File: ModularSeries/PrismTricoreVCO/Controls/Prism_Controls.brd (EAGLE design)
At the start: 48.5 x 100 mm, 10 parts

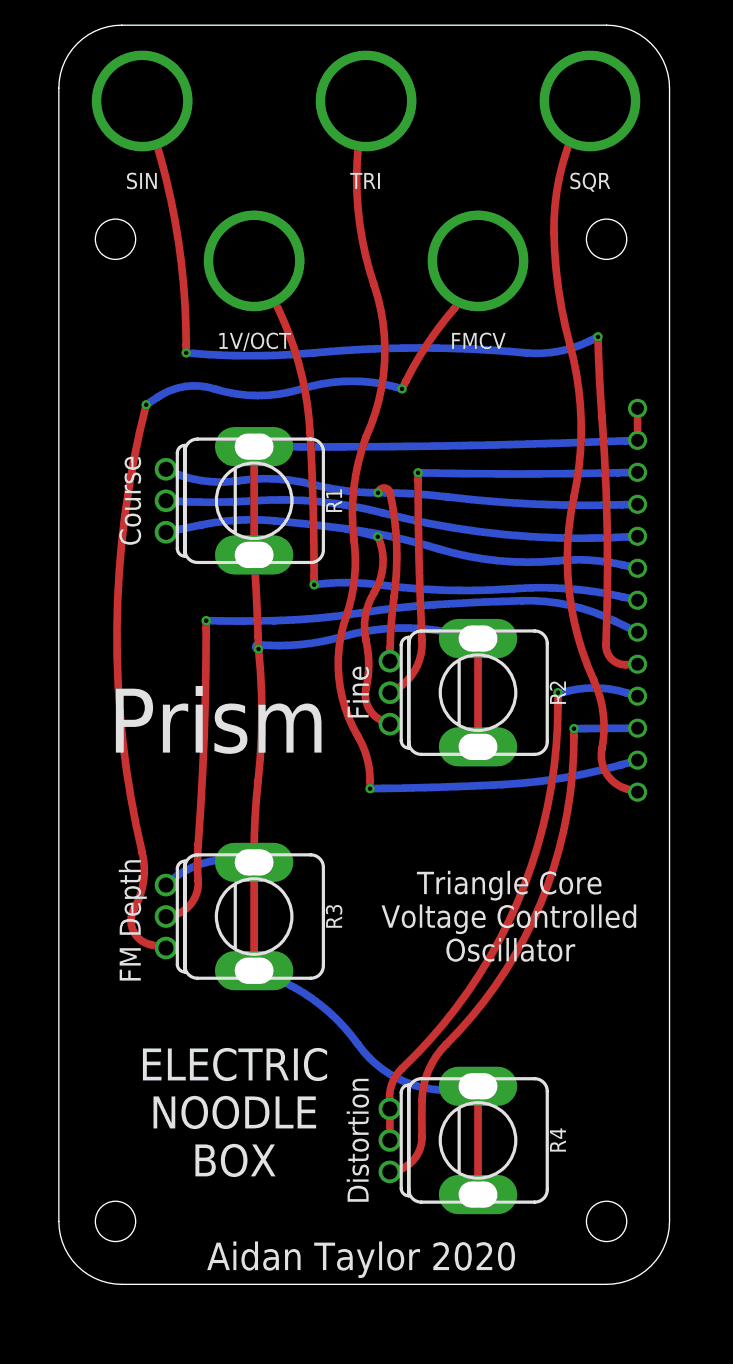
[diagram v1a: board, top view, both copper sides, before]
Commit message: Prism control card updated to accomodate Cinch nanas
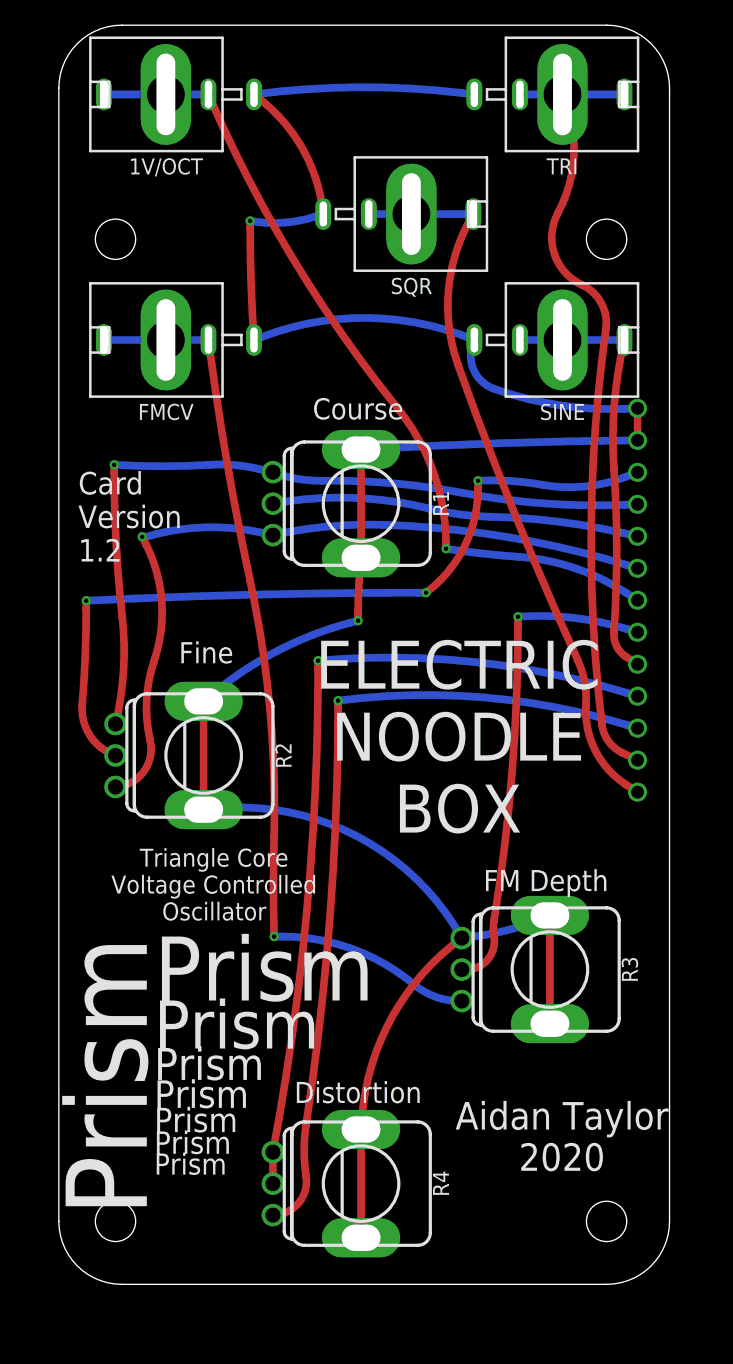
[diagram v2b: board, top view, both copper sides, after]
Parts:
- removed SIN: BANANA_PANEL, ElectricNoodleBox:BANANA_PANEL
- added SINE: COMBI-JACKCINCHNANA, ElectricNoodleBox:NEWCOMBOJACK_PANEL
- 1V/OCT, FMCV, SQR, TRI: value BANANA_PANEL -> COMBI-JACKCINCHNANA; device ElectricNoodleBox:BANANA_PANEL -> ElectricNoodleBox:NEWCOMBOJACK_PANEL
- moved FMCV 25.6 mm to (9.50, 75.0), turned to 90 degrees
- moved R3 23.9 mm to (40.0, 25.0)
- moved R2 22.4 mm to (12.5, 42.0)
- moved SQR 16.8 mm to (29.0, 85.0), turned to 270 degrees
- moved TRI 15.6 mm to (41.0, 94.5), turned to 270 degrees
- moved 1V/OCT 15.0 mm to (9.50, 94.5), turned to 90 degrees
- moved R4 9.90 mm to (25.0, 8.00)
- moved R1 8.49 mm to (25.0, 62.0)
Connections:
- net AGND: now also 1V/OCT.S, FMCV.S, SINE.S, SQR.S, TRI.S
- net N$1: now also 1V/OCT.T1, 1V/OCT.T2
- net N$10: now also SINE.CONN, SINE.T1, SINE.T2; no longer SIN.CONN
- net N$11: now also TRI.T1, TRI.T2
- net N$12: now also SQR.T1, SQR.T2
- net N$6: now also FMCV.T1, FMCV.T2
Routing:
- net AGND: track 137.4 -> 202.4 mm, vias 1 -> 2
- net N$10: track 80.8 -> 34.8 mm, vias 2 -> 0
- net N$5: track 35.6 -> 62.7 mm, vias 1 -> 3
- net N$8: track 44.6 -> 67.2 mm
- net N$9: track 43.7 -> 65.8 mm
- net N$7: track 59.2 -> 38.7 mm
- net N$11: track 76.3 -> 63.3 mm, vias 1 -> 0
- net N$1: track 52.2 -> 65.1 mm
- net N$2: track 51.9 -> 62.4 mm
- net N$4: track 37.6 -> 29.1 mm
- net N$6: track 76.9 -> 71.8 mm, vias 2 -> 1
- net N$3: track 56.1 -> 60.6 mm
- net N$12: track 56.7 -> 57.4 mm
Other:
- board text added: "Card Version 1.2"

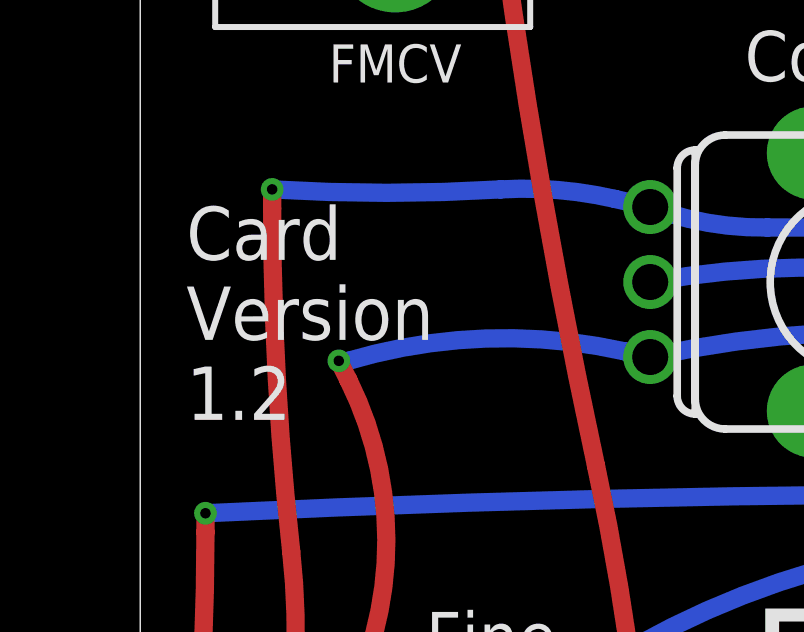
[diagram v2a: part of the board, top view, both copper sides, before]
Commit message: Updates to Portals and Knives, Panel layout for Prism and Knives added
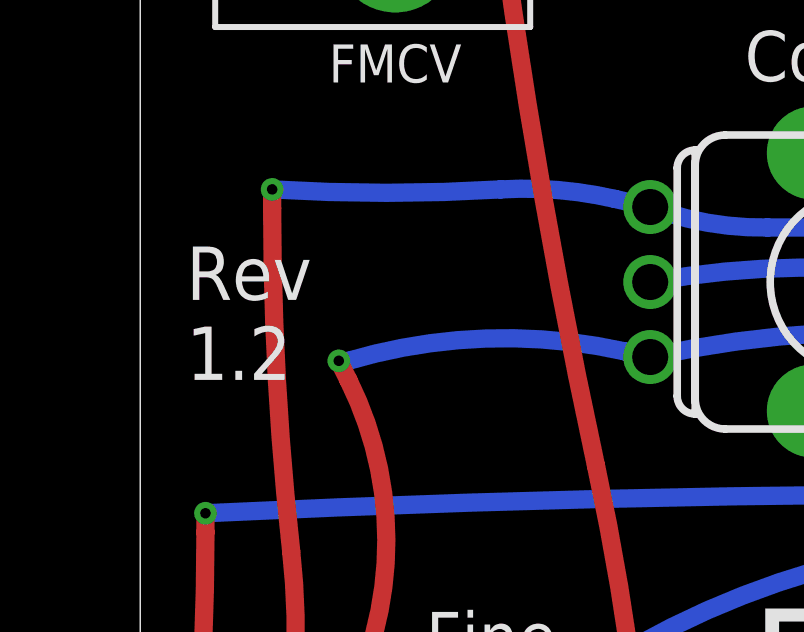
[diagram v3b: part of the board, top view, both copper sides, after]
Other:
- board text added: "Rev 1.2"
- board text removed: "Card Version 1.2"
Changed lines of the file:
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@@
 <setting verticaltext="up"/>
 </settings>
-<grid distance="12.5" unitdist="mil" unit="mil" style="lines" multiple="1" display="no" altdistance="5" altunitdist="mil" altunit="mil"/>
+<grid distance="12.5" unitdist="mil" unit="mm" style="lines" multiple="1" display="no" altdistance="5" altunitdist="mil" altunit="mil"/>
 <layers>
 <layer number="1" name="Top" color="4" fill="1" visible="yes" active="yes"/>
@@
 <layer number="44" name="Drills" color="7" fill="1" visible="no" active="yes"/>
 <layer number="45" name="Holes" color="7" fill="1" visible="no" active="yes"/>
-<layer number="46" name="Milling" color="3" fill="1" visible="no" active="yes"/>
+<layer number="46" name="Milling" color="3" fill="1" visible="yes" active="yes"/>
 <layer number="47" name="Measures" color="7" fill="1" visible="no" active="yes"/>
 <layer number="48" name="Document" color="7" fill="1" visible="yes" active="yes"/>
@@
 </layers>
 <board>
-<fusionsync huburn="a.cGVyc29uYWw6dWUyYjdlNGE0" projecturn="a.cGVyc29uYWw6dWUyYjdlNGE0IzIwMjAwNDA1MjgzMzA0MTgx" f3durn="urn:adsk.wipprod:dm.lineage:eztbtJ9iQJeDtqV6BqPWgw" pcbguid="61dd8330-7d56-4479-a556-bfe94448c2a6" lastpulledtime="" lastsyncedchangeguid="" latestrevisionid="f6234553-8fbd-4fc4-b8d3-3ce2f196028d" lastsyncedrevisionid="f6234553-8fbd-4fc4-b8d3-3ce2f196028d" lastboardhashguid="e6fa3100-0058-71b5-b3eb-78c96a5d02e4" lastpushedtime="2020-05-27T16:03:25Z" linktopcb3d="%12"/>
 <plain>
 <wire x1="1" y1="95" x2="1" y2="5" width="0" layer="20"/>
@@
 <text x="8.5725" y="11.255" size="1.778" layer="21" font="vector" ratio="16" rot="R180" align="center-right">Prism</text>
 <text x="8.5725" y="9.555" size="1.6764" layer="21" font="vector" ratio="16" rot="R180" align="center-right">Prism</text>
-<text x="2.54" y="60.96" size="1.778" layer="21" font="vector" ratio="12" align="center-left">Card
-Version
+<text x="2.54" y="60.96" size="1.778" layer="21" font="vector" ratio="12" align="center-left">Rev
 1.2</text>
 </plain>
@@
 which will not be processed correctly with this version.
 </note>
-<note version="8.3" severity="warning">
-Since Version 8.3, EAGLE supports Fusion synchronisation.
-This feature will not be available in this version and saving
-the document will break the link to the Fusion PCB feature.
-</note>
 </compatibility>

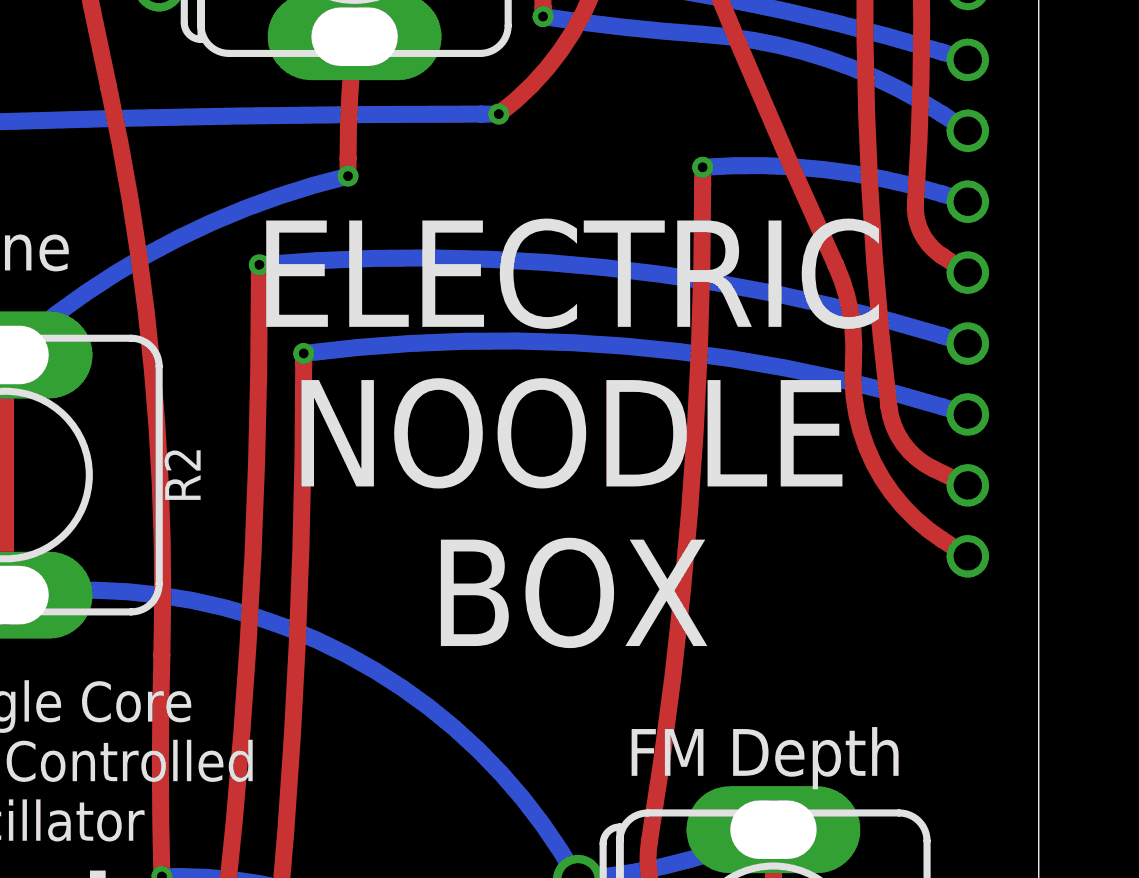
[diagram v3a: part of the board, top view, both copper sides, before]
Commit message: Panel for TimeSeeds added. TLHP core PCB added
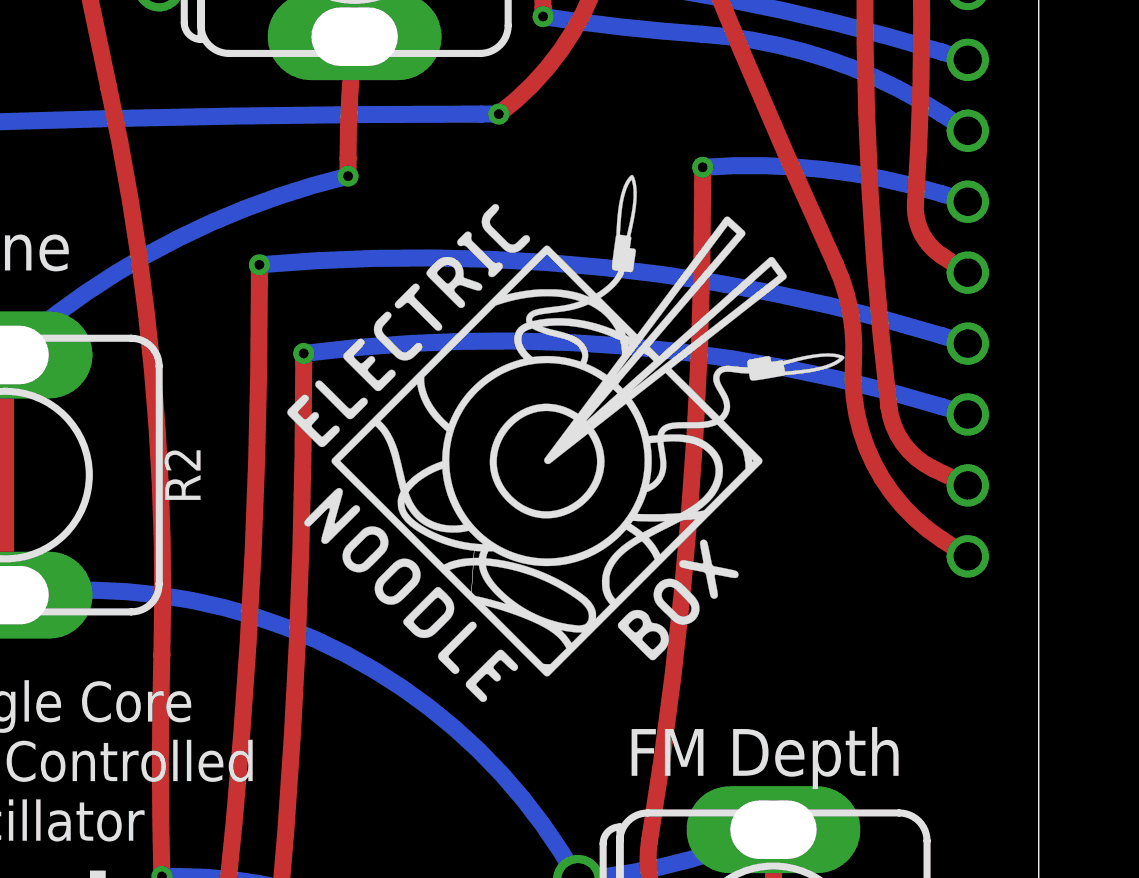
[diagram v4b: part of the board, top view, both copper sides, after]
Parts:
- added U$1, U$2: (no value), ElectricNoodleBox:LOGO20X20
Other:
- board text removed: "ELECTRIC NOODLE BOX"
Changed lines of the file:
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@@
 <?xml version="1.0" encoding="utf-8"?>
 <!DOCTYPE eagle SYSTEM "eagle.dtd">
-<eagle version="9.6.0">
+<eagle version="9.6.2">
 <drawing>
 <settings>
@@
 </layers>
 <board>
+<fusionsync huburn="a.cGVyc29uYWw6dWUyYjdlNGE0" projecturn="a.cGVyc29uYWw6dWUyYjdlNGE0IzIwMjAwNDA1MjgzMzA0MTgx" f3durn="urn:adsk.wipprod:dm.lineage:d43Js7DXSPm0I4Y9FW37gw" pcbguid="bb15d56c-a622-4132-a217-e5fd2946aa94" lastpulledtime="" lastsyncedchangeguid="" latestrevisionid="eb549d52-2273-4d8d-8620-3ff576db5721" lastsyncedrevisionid="eb549d52-2273-4d8d-8620-3ff576db5721" lastboardhashguid="821108dc-9c2e-e31c-5548-4e48dbdf034a" lastpushedtime="2020-06-25T11:06:21Z" linktopcb3d="true"/>
 <plain>
 <wire x1="1" y1="95" x2="1" y2="5" width="0" layer="20"/>
@@
 Oscillator</text>
 <text x="4.7625" y="27.6225" size="6.4516" layer="21" font="vector" ratio="16" rot="R90" align="center-right">Prism</text>
-<text x="32.7025" y="43.4975" size="3.81" layer="21" font="vector" ratio="16" align="center">ELECTRIC
-NOODLE
-BOX</text>
 <text x="40.9575" y="11.7475" size="2.1844" layer="21" font="vector" ratio="16" align="center">Aidan Taylor
 2020</text>
@@
 <attribute name="NAME" x="29" y="79.285" size="1.27" layer="25" font="vector" align="center"/>
 </element>
+<element name="U$1" library="ElectricNoodleBox" package="LOGO20X20" value="" x="22.5425" y="33.3375" smashed="yes"/>
+<element name="U$2" library="ElectricNoodleBox" package="LOGO20X20" value="" x="41.275" y="33.3375" smashed="yes" rot="MR0"/>
 </elements>
 <signals>
@@
 which will not be processed correctly with this version.
 </note>
+<note version="8.3" severity="warning">
+Since Version 8.3, EAGLE supports Fusion synchronisation.
+This feature will not be available in this version and saving
+the document will break the link to the Fusion PCB feature.
+</note>
 </compatibility>

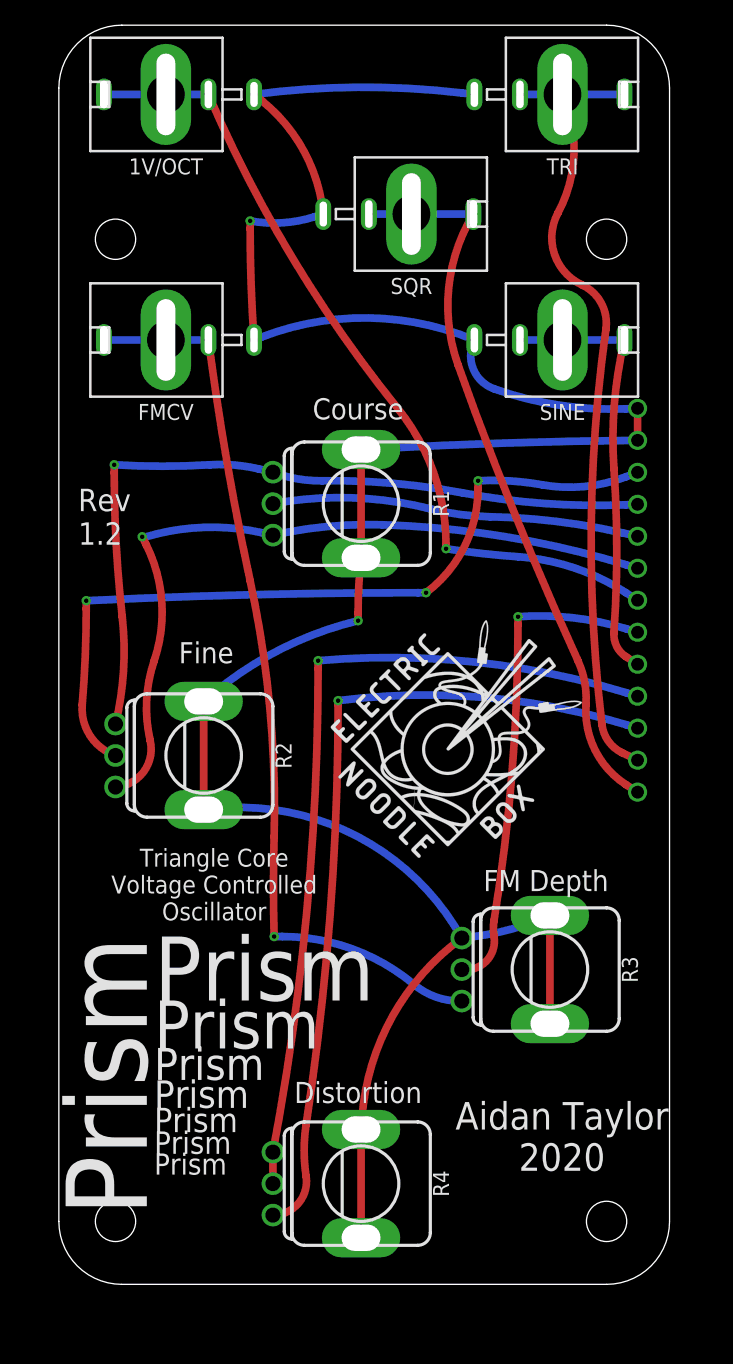
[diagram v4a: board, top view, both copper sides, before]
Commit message: Layout and schematic renders for LHP added
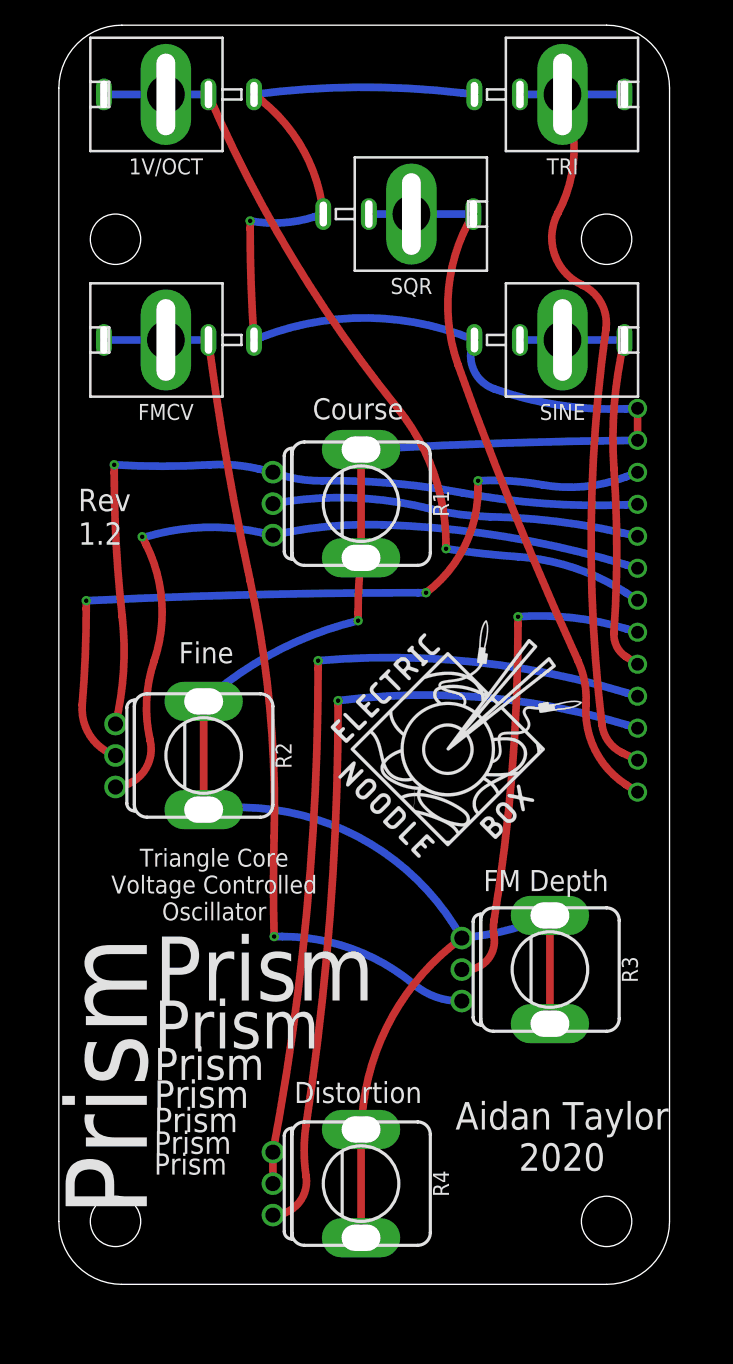
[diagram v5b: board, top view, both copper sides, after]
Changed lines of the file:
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@@
 </layers>
 <board>
-<fusionsync huburn="a.cGVyc29uYWw6dWUyYjdlNGE0" projecturn="a.cGVyc29uYWw6dWUyYjdlNGE0IzIwMjAwNDA1MjgzMzA0MTgx" f3durn="urn:adsk.wipprod:dm.lineage:d43Js7DXSPm0I4Y9FW37gw" pcbguid="bb15d56c-a622-4132-a217-e5fd2946aa94" lastpulledtime="" lastsyncedchangeguid="" latestrevisionid="eb549d52-2273-4d8d-8620-3ff576db5721" lastsyncedrevisionid="eb549d52-2273-4d8d-8620-3ff576db5721" lastboardhashguid="821108dc-9c2e-e31c-5548-4e48dbdf034a" lastpushedtime="2020-06-25T11:06:21Z" linktopcb3d="true"/>
+<fusionsync huburn="a.cGVyc29uYWw6dWUyYjdlNGE0" projecturn="a.cGVyc29uYWw6dWUyYjdlNGE0IzIwMjAwNDA1MjgzMzA0MTgx" f3durn="urn:adsk.wipprod:dm.lineage:d43Js7DXSPm0I4Y9FW37gw" pcbguid="" lastpulledtime="" lastsyncedchangeguid="" latestrevisionid="eb549d52-2273-4d8d-8620-3ff576db5721" lastsyncedrevisionid="eb549d52-2273-4d8d-8620-3ff576db5721" lastboardhashguid="821108dc-9c2e-e31c-5548-4e48dbdf034a" lastpushedtime="2020-06-25T11:06:21Z" linktopcb3d="true"/>
 <plain>
 <wire x1="1" y1="95" x2="1" y2="5" width="0" layer="20"/>
